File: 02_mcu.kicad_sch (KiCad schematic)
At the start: 31 parts, among them J2 0533980571, U3 MSPM0C1104SDDFR, U4 TLC59208F, U5 VEML7700, U6 TLV803E

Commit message: Add MPN and DigiKey PN to all components
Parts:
- C10, C12, C13: DigiKey PN (none) -> 1276-6720-1-ND; MPN (none) -> CL05B104KA5NNNC
- C11: DigiKey PN (none) -> 1276-1804-1-ND
- D10, D11: DigiKey PN (none) -> 1497-1354-ND
- D12: DigiKey PN (none) -> 497-7746-1-ND; MPN (none) -> ESDA5V3SC5
- D4, D5, D6: DigiKey PN (none) -> 1497-XLVG12D-ND
- D7, D8, D9: DigiKey PN (none) -> XLMYK12D-ND
- J2: DigiKey PN (none) -> WM7609CT-ND; MPN (none) -> 0533980571
- R10, R11, R12, R13, R14, R15, R7, R8: DigiKey PN (none) -> 311-68.0LRCT-ND; MPN (none) -> RC0402FR-0768RL
- R5, R6: DigiKey PN (none) -> 13-RC0402FR-133K3LCT-ND; MPN (none) -> RC0402FR-133K3L
- R9: DigiKey PN (none) -> 311-5.6KLRCT-ND; MPN (none) -> RC0402FR-075K6L
- U3: DigiKey PN (none) -> 296-MSPM0C1104SDDFRCT-ND; MPN (none) -> MSPM0C1104SDDFR
- U4: DigiKey PN (none) -> 296-36989-1-ND; MPN (none) -> TLC59208FIRGYR
- U5: DigiKey PN (none) -> VEML7700CT-ND; MPN (none) -> VEML7700-TR
- U6: DigiKey PN (none) -> 296-TLV803ED29DBZRCT-ND

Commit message: Schematic: Update comments for I2c addresses of devices
Fix incorrect address for LED driver and add address of ambient light
sensor.
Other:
- note added: "I2C addr: 0x10"
- note added: "I2C addr: 0x20"
- note removed: "I2C addr: 0x40"
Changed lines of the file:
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@@
 		)
 	)
-	(text "I2C addr: 0x40"
+	(text "I2C addr: 0x20"
 		(exclude_from_sim no)
 		(at 182.245 100.965 0)
 		(effects
 			(font
+				(size 1.27 1.27)
+			)
+		)
+	)
+	(text "I2C addr: 0x10"
+		(exclude_from_sim no)
+		(at 147.32 159.385 0)
+		(effects
+			(font

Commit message: Fix swapped SCL and SDA pins for VEML7700
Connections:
- net I2C_SCL: now also U5.1 (SCL); no longer U5.4 (SDA)
- net I2C_SDA: now also U5.4 (SDA); no longer U5.1 (SCL)

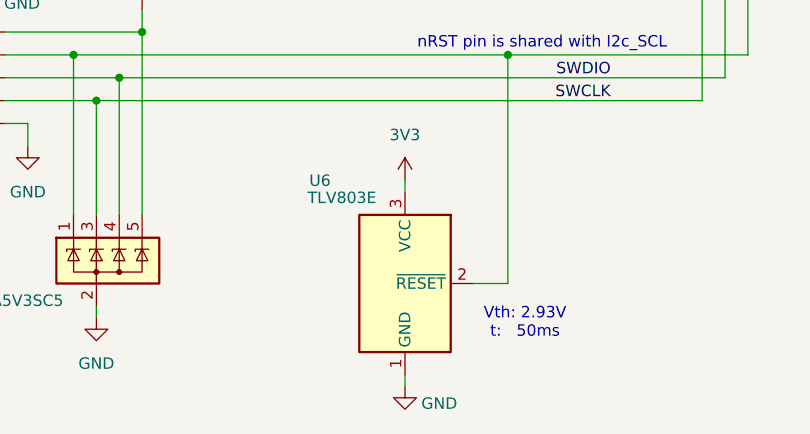
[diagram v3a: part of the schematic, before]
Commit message: Fix wrong footprint for TLV803E
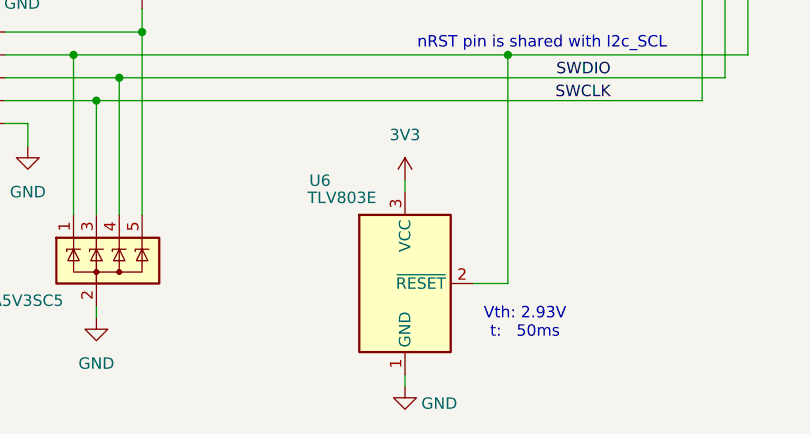
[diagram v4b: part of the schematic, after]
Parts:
- U6: footprint Package_TO_SOT_SMD:SOT-323_SC-70 -> Package_TO_SOT_SMD:SOT-23
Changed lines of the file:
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@@
 			)
 		)
-		(property "Footprint" "Package_TO_SOT_SMD:SOT-323_SC-70"
+		(property "Footprint" "Package_TO_SOT_SMD:SOT-23"
 			(at 90.17 152.4 0)
 			(effects
@@
 			)
 		)
-		(property "Description" "Microprocessor Reset (active-low) Circuit, SOT-323"
+		(property "Description" "Microprocessor Reset (active-low) Circuit, SOT-23"
 			(at 82.55 154.94 0)
 			(effects
